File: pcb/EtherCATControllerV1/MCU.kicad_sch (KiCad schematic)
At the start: 10 parts, among them U1 STM32F405RGT6, Y1 ABM3B-8.000MHZ-10-1-U-T

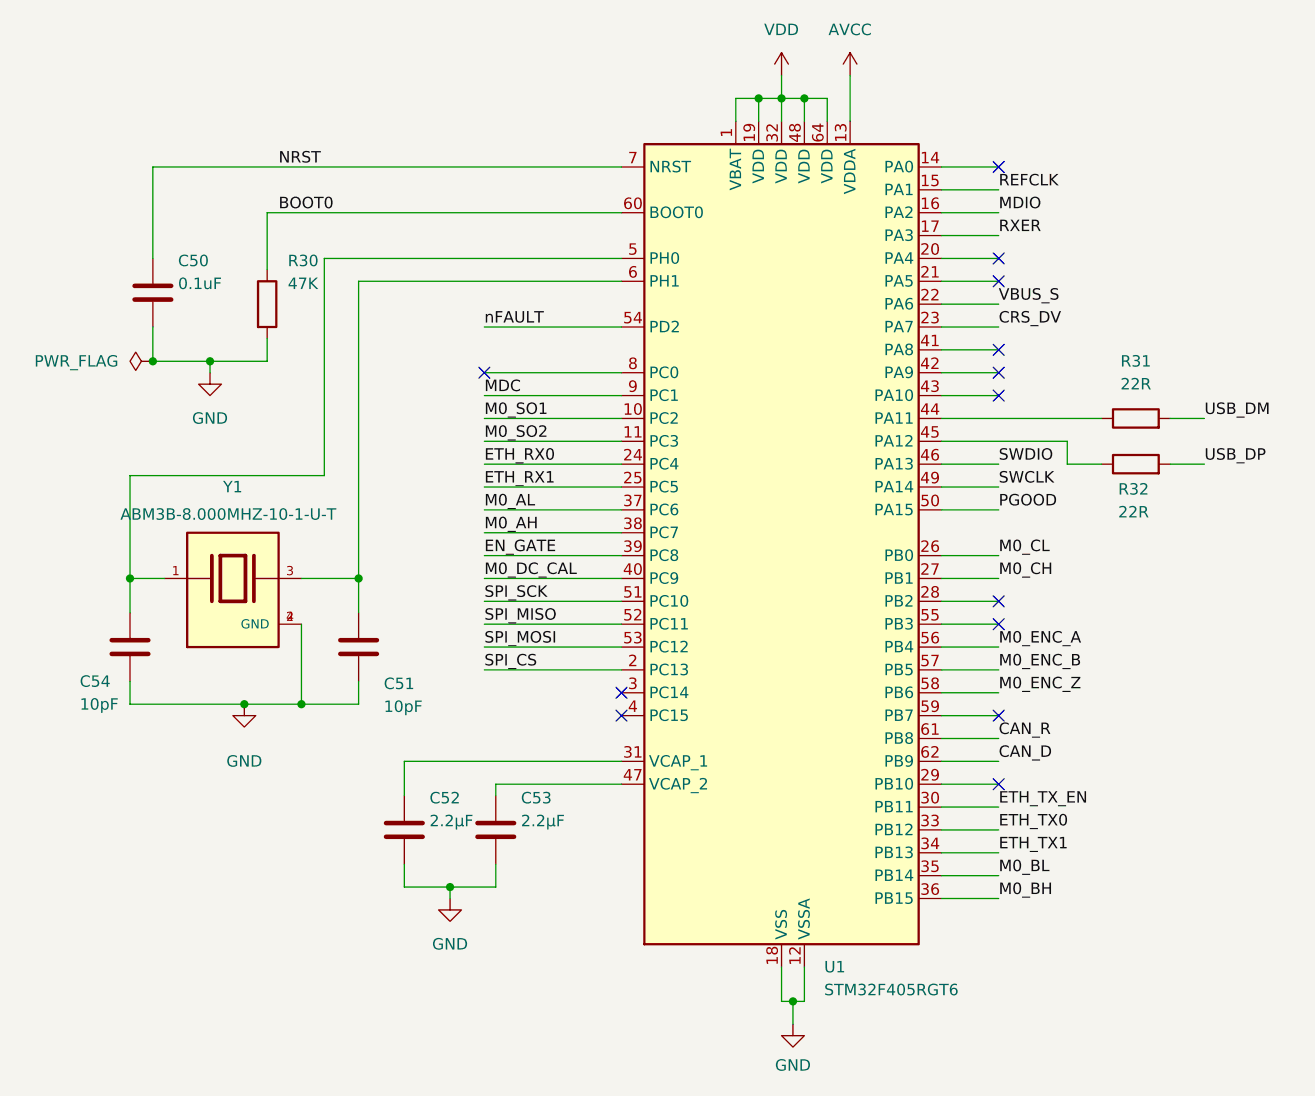
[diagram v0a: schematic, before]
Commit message: Initial design without Ethernet connectors
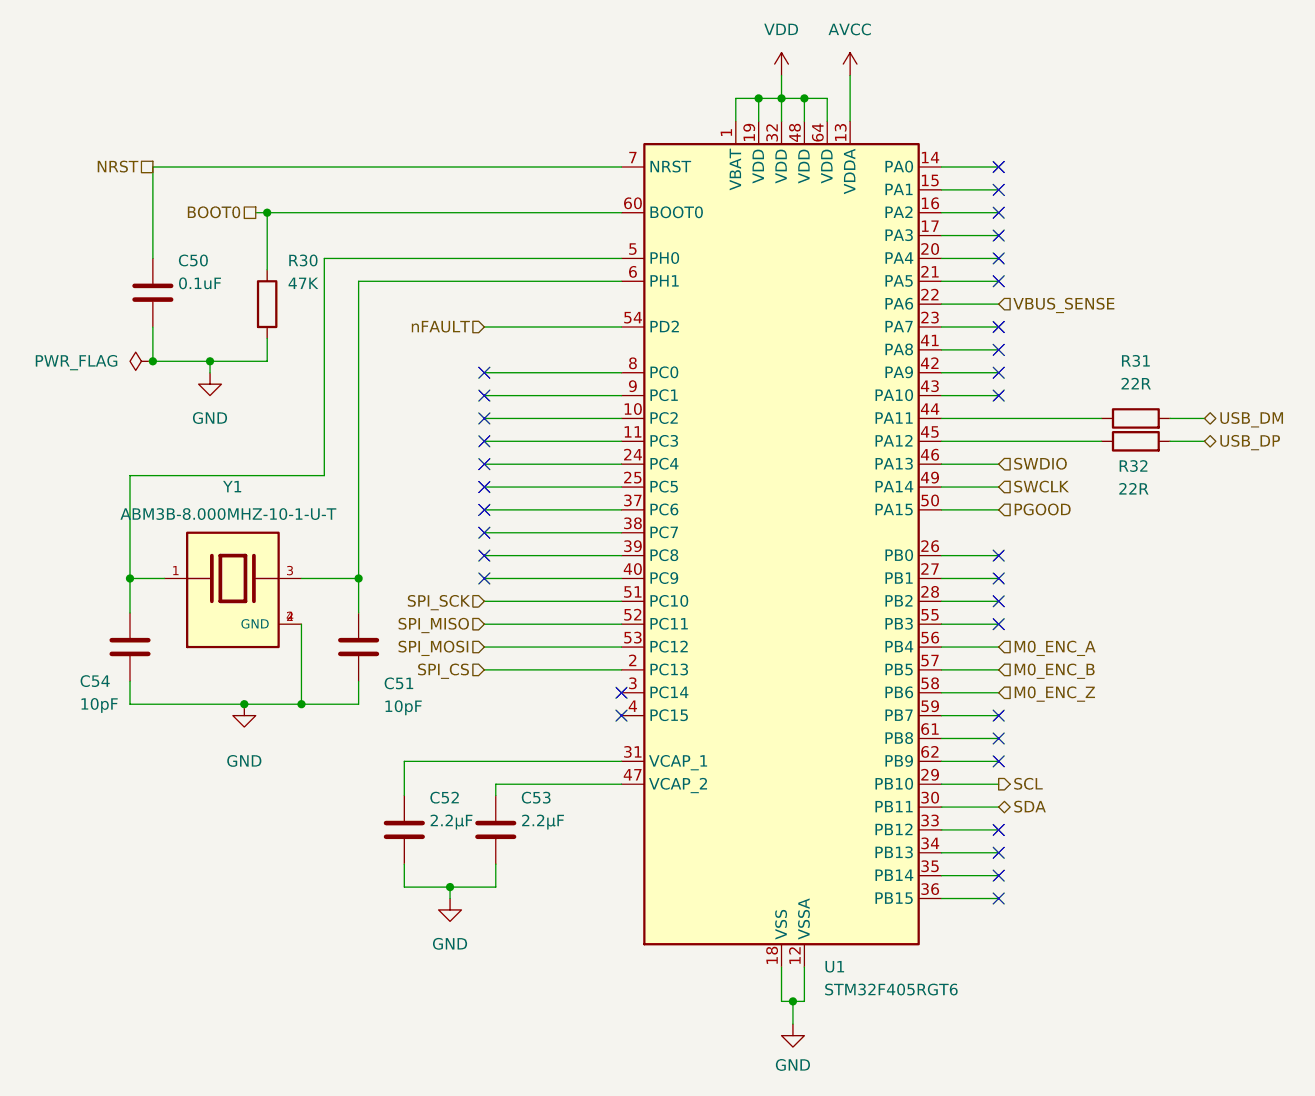
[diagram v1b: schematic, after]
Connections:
- net SCL: now reaches U1.29 (PB10)
- net CAN_D: no longer names the net of U1.62 (PB9)
- net CAN_R: no longer names the net of U1.61 (PB8)
- net CRS_DV: no longer names the net of U1.23 (PA7)
- net EN_GATE: no longer names the net of U1.39 (PC8)
- net ETH_RX0: no longer names the net of U1.24 (PC4)
- net ETH_RX1: no longer names the net of U1.25 (PC5)
- net ETH_TX0: no longer names the net of U1.33 (PB12)
- net ETH_TX1: no longer names the net of U1.34 (PB13)
- net ETH_TX_EN renamed SDA
- net M0_AH: no longer names the net of U1.38 (PC7)
- net M0_AL: no longer names the net of U1.37 (PC6)
- net M0_BH: no longer names the net of U1.36 (PB15)
- net M0_BL: no longer names the net of U1.35 (PB14)
- net M0_CH: no longer names the net of U1.27 (PB1)
- net M0_CL: no longer names the net of U1.26 (PB0)
- net M0_DC_CAL: no longer names the net of U1.40 (PC9)
- net M0_SO1: no longer names the net of U1.10 (PC2)
- net M0_SO2: no longer names the net of U1.11 (PC3)
- net MDC: no longer names the net of U1.9 (PC1)
- net MDIO: no longer names the net of U1.16 (PA2)
- net REFCLK: no longer names the net of U1.15 (PA1)
- net RXER: no longer names the net of U1.17 (PA3)
- net VBUS_S renamed VBUS_SENSE
- no-connect marks 13 -> 33
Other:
- moved on the sheet: R32

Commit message: schematic finished, need to set proper ERCs
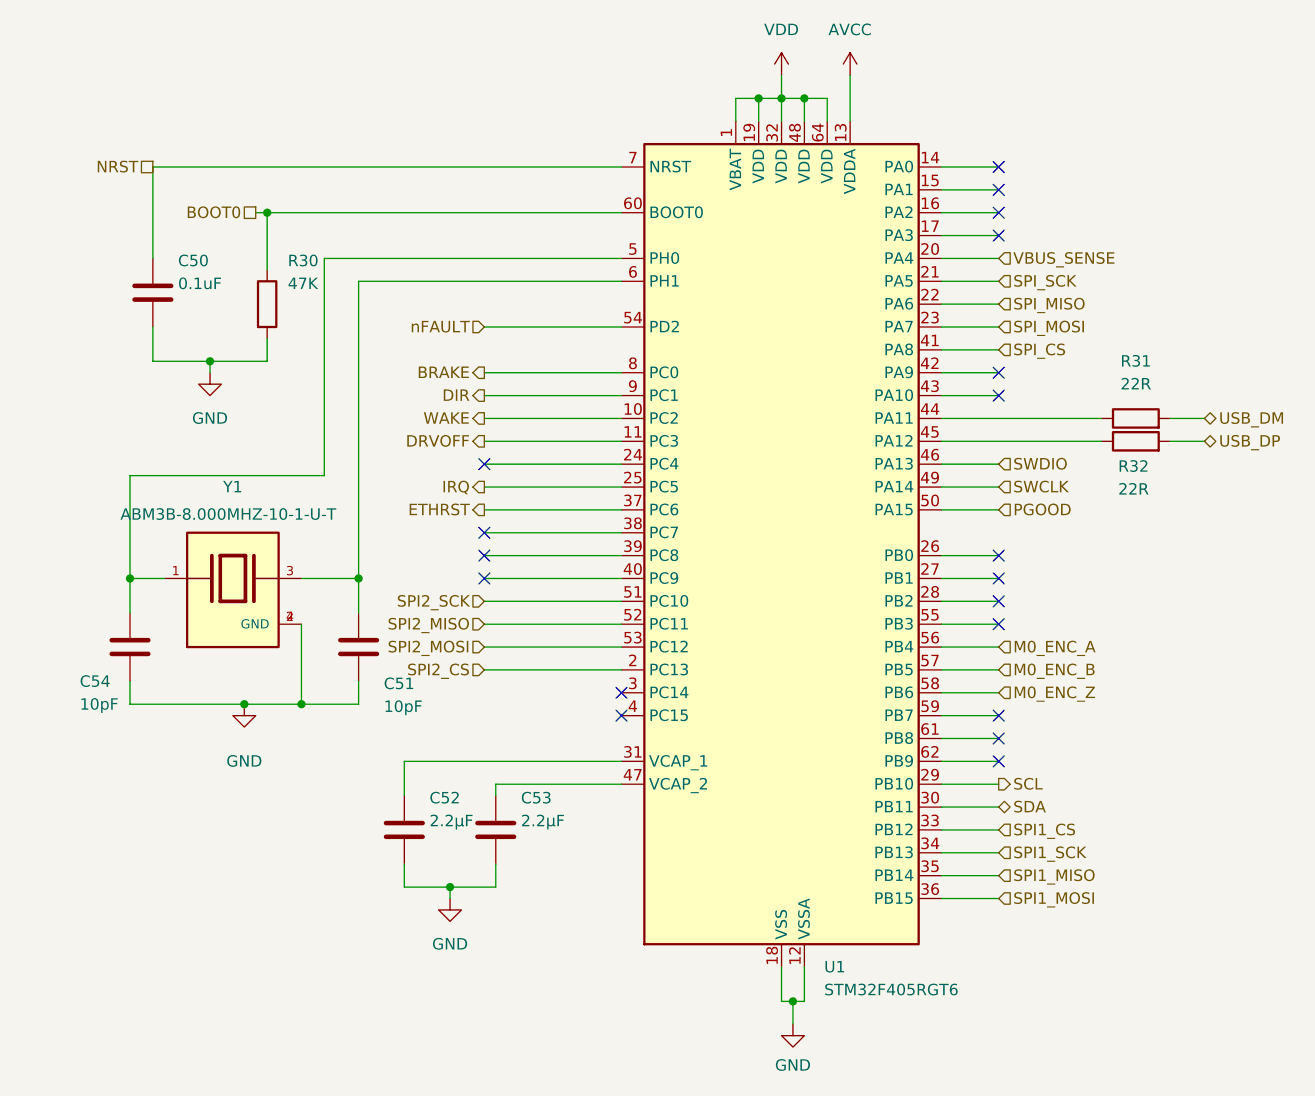
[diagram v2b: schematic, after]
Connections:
- net SPI_CS: now also U1.41 (PA8); no longer U1.2 (PC13)
- net SPI_MISO: now also U1.22 (PA6); no longer U1.52 (PC11)
- net SPI_MOSI: now also U1.23 (PA7); no longer U1.53 (PC12)
- net SPI_SCK: now also U1.21 (PA5); no longer U1.51 (PC10)
- net VBUS_SENSE: now also U1.20 (PA4); no longer U1.22 (PA6)
- net WAKE: now reaches U1.10 (PC2)
- net DRVOFF: now reaches U1.11 (PC3)
- net IRQ: now reaches U1.25 (PC5)
- net SPI1_CS: now reaches U1.33 (PB12)
- net SPI1_SCK: now reaches U1.34 (PB13)
- net SPI1_MISO: now reaches U1.35 (PB14)
- net SPI1_MOSI: now reaches U1.36 (PB15)
- net ETHRST: now reaches U1.37 (PC6)
- net BRAKE: now reaches U1.8 (PC0)
- net DIR: now reaches U1.9 (PC1)
- new net SPI2_CS: U1.2 (PC13)
- new net SPI2_MISO: U1.52 (PC11)
- new net SPI2_MOSI: U1.53 (PC12)
- new net SPI2_SCK: U1.51 (PC10)
- no-connect marks 33 -> 19
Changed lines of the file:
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@@
-	)
-	(junction
-		(at 76.2 60.96)
-		(diameter 0)
-		(color 0 0 0 0)
 	)
 	(junction
@@
 	)
 	(no_connect
-		(at 170.18 49.53)
-	)
-	(no_connect
 		(at 170.18 85.09)
 	)
@@
 	)
 	(no_connect
-		(at 170.18 115.57)
-	)
-	(no_connect
-		(at 113.03 74.93)
-	)
-	(no_connect
 		(at 113.03 85.09)
 	)
@@
 	)
 	(no_connect
-		(at 113.03 67.31)
-	)
-	(no_connect
-		(at 113.03 69.85)
-	)
-	(no_connect
-		(at 113.03 62.23)
-	)
-	(no_connect
-		(at 170.18 118.11)
-	)
-	(no_connect
-		(at 170.18 52.07)
-	)
-	(no_connect
 		(at 170.18 41.91)
-	)
-	(no_connect
-		(at 170.18 120.65)
 	)
 	(no_connect
@@
 	)
 	(no_connect
-		(at 170.18 59.69)
-	)
-	(no_connect
 		(at 170.18 46.99)
 	)
@@
 	)
 	(no_connect
-		(at 113.03 77.47)
-	)
-	(no_connect
-		(at 113.03 64.77)
-	)
-	(no_connect
 		(at 113.03 82.55)
-	)
-	(no_connect
-		(at 170.18 113.03)
 	)
 	(no_connect
@@
 	(no_connect
 		(at 170.18 62.23)
-	)
-	(no_connect
-		(at 170.18 57.15)
 	)
 	(no_connect
@@
 		)
 	)
-	(hierarchical_label "VBUS_SENSE"
+	(hierarchical_label "DRVOFF"
+		(shape output)
+		(at 113.03 69.85 180)
+		(fields_autoplaced yes)
+		(effects
+			(font
+				(size 1.27 1.27)
+			)
+			(justify right)
+		)
+	)
+	(hierarchical_label "SPI1_SCK"
 		(shape input)
-		(at 170.18 54.61 0)
+		(at 170.18 115.57 0)
+		(fields_autoplaced yes)
+		(effects
+			(font
+				(size 1.27 1.27)
+			)
+			(justify left)
+		)
+	)
+	(hierarchical_label "ETHRST"
+		(shape output)
+		(at 113.03 77.47 180)
+		(fields_autoplaced yes)
+		(effects
+			(font
+				(size 1.27 1.27)
+			)
+			(justify right)
+		)
+	)
+	(hierarchical_label "DIR"
+		(shape output)
+		(at 113.03 64.77 180)
+		(fields_autoplaced yes)
+		(effects
+			(font
+				(size 1.27 1.27)
+			)
+			(justify right)
+		)
+	)
+	(hierarchical_label "SDA"
+		(shape bidirectional)
+		(at 170.18 110.49 0)
 		(fields_autoplaced yes)
 		(effects
@@
 		)
 	)
+	(hierarchical_label "SPI2_SCK"
+		(shape input)
+		(at 113.03 87.63 180)
+		(fields_autoplaced yes)
+		(effects
+			(font
+				(size 1.27 1.27)
+			)
+			(justify right)
+		)
+	)
 	(hierarchical_label "SPI_SCK"
 		(shape input)
-		(at 113.03 87.63 180)
-		(fields_autoplaced yes)
-		(effects
-			(font
-				(size 1.27 1.27)
-			)
-			(justify right)
+		(at 170.18 52.07 0)
+		(fields_autoplaced yes)
+		(effects
+			(font
+				(size 1.27 1.27)
+			)
+			(justify left)
 		)
 	)
@@
 		)
 	)
+	(hierarchical_label "IRQ"
+		(shape output)
+		(at 113.03 74.93 180)
+		(fields_autoplaced yes)
+		(effects
+			(font
+				(size 1.27 1.27)
+			)
+			(justify right)
+		)
+	)
+	(hierarchical_label "SPI1_MISO"
+		(shape input)
+		(at 170.18 118.11 0)
+		(fields_autoplaced yes)
+		(effects
+			(font
+				(size 1.27 1.27)
+			)
+			(justify left)
+		)
+	)
+	(hierarchical_label "WAKE"
+		(shape output)
+		(at 113.03 67.31 180)
+		(fields_autoplaced yes)
+		(effects
+			(font
+				(size 1.27 1.27)
+			)
+			(justify right)
+		)
+	)
+	(hierarchical_label "VBUS_SENSE"
+		(shape input)
+		(at 170.18 49.53 0)
+		(fields_autoplaced yes)
+		(effects
+			(font
+				(size 1.27 1.27)
+			)
+			(justify left)
+		)
+	)
+	(hierarchical_label "SWCLK"
+		(shape input)
+		(at 170.18 74.93 0)
+		(fields_autoplaced yes)
+		(effects
+			(font
+				(size 1.27 1.27)
+			)
+			(justify left)
+		)
+	)
 	(hierarchical_label "SCL"
 		(shape output)
@@
 		)
 	)
-	(hierarchical_label "SWCLK"
+	(hierarchical_label "SPI1_CS"
 		(shape input)
-		(at 170.18 74.93 0)
+		(at 170.18 113.03 0)
+		(fields_autoplaced yes)
+		(effects
+			(font
+				(size 1.27 1.27)
+			)
+			(justify left)
+		)
+	)
+	(hierarchical_label "BRAKE"
+		(shape output)
+		(at 113.03 62.23 180)
+		(fields_autoplaced yes)
+		(effects
+			(font
+				(size 1.27 1.27)
+			)
+			(justify right)
+		)
+	)
+	(hierarchical_label "SPI_CS"
+		(shape input)
+		(at 170.18 59.69 0)
 		(fields_autoplaced yes)
 		(effects
@@
 		)
 	)
-	(hierarchical_label "SPI_MISO"
+	(hierarchical_label "SPI2_MISO"
 		(shape input)
 		(at 113.03 90.17 180)
@@
 		)
 	)
-	(hierarchical_label "SPI_CS"
+	(hierarchical_label "SPI_MOSI"
+		(shape input)
+		(at 170.18 57.15 0)
+		(fields_autoplaced yes)
+		(effects
+			(font
+				(size 1.27 1.27)
+			)
+			(justify left)
+		)
+	)
+	(hierarchical_label "SPI2_CS"
 		(shape input)
 		(at 113.03 95.25 180)
@@
 		)
 	)
-	(hierarchical_label "SPI_MOSI"
+	(hierarchical_label "SPI2_MOSI"
 		(shape input)
 		(at 113.03 92.71 180)
@@
 		)
 	)
-	(hierarchical_label "SDA"
-		(shape bidirectional)
-		(at 170.18 110.49 0)
+	(hierarchical_label "SPI_MISO"
+		(shape input)
+		(at 170.18 54.61 0)
 		(fields_autoplaced yes)
 		(effects
@@
 		(shape input)
 		(at 170.18 95.25 0)
+		(fields_autoplaced yes)
+		(effects
+			(font
+				(size 1.27 1.27)
+			)
+			(justify left)
+		)
+	)
+	(hierarchical_label "SPI1_MOSI"
+		(shape input)
+		(at 170.18 120.65 0)
 		(fields_autoplaced yes)
 		(effects
@@
 					(unit 1)
 				)
-			)
-		)
-	)
-	(symbol
-		(lib_id "power:PWR_FLAG")
-		(at 76.2 60.96 90)
-		(unit 1)
-		(exclude_from_sim no)
-		(in_bom yes)
-		(on_board yes)
-		(dnp no)
-		(property "Reference" "#FLG03"
-			(at 74.295 60.96 0)
-			(effects
-				(font
-					(size 1.27 1.27)
-				)
-				(hide yes)
-			)
-		)
-		(property "Value" "PWR_FLAG"
-			(at 72.39 60.9599 90)
-			(effects
-				(font
-					(size 1.27 1.27)
-				)
-				(justify left)
-			)
-		)
-		(property "Footprint" ""
-			(at 76.2 60.96 0)
-			(effects
-				(font
-					(size 1.27 1.27)
-				)
-				(hide yes)
-			)
-		)
-		(property "Datasheet" "~"
-			(at 76.2 60.96 0)
-			(effects
-				(font
-					(size 1.27 1.27)
-				)
-				(hide yes)
-			)
-		)
-		(property "Description" "Special symbol for telling ERC where power comes from"
-			(at 76.2 60.96 0)
-			(effects
-				(font
-					(size 1.27 1.27)
-				)
-				(hide yes)
-			)
-		)
-		(pin "1"
-		)
-		(instances
-			(project "EtherCATControllerV1"
-				(path "/4c927f80-855d-490a-80b2-e5c55283621a/c856d8b8-b384-4f6b-bd82-a15acb88b807"
-					(reference "#FLG03")
-					(unit 1)
-				)

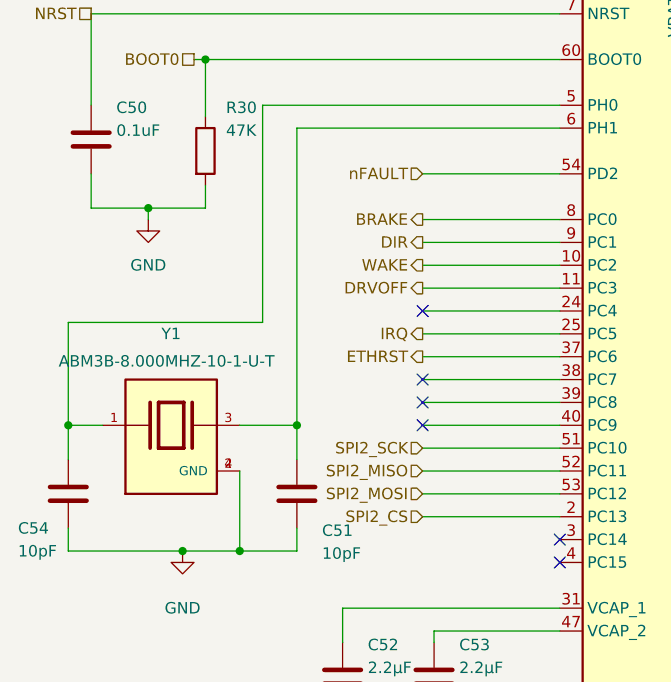
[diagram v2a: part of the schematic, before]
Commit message: Added more BOM items
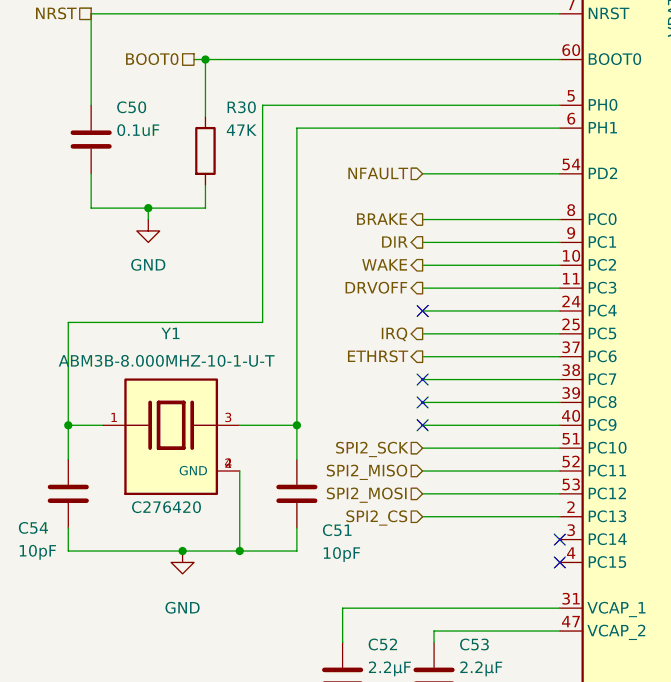
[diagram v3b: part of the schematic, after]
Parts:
- Y1: LCSC Part Number (none) -> C276420
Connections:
- net nFAULT renamed NFAULT
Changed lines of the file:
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@@
 		)
 	)
-	(hierarchical_label "nFAULT"
+	(hierarchical_label "NFAULT"
 		(shape input)
 		(at 113.03 57.15 180)
@@
 			)
 		)
+		(property "LCSC Part Number" " C276420"
+			(at 84.582 94.234 0)
+			(effects
+				(font
+					(size 1.27 1.27)
+				)
+			)
+		)
